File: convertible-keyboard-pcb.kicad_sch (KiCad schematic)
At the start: 216 parts, among them SW1 SW_MX_LED, SW10 SW_MX_LED, SW100 SW_MX_LED, SW101 SW_MX_LED, SW102 SW_MX_LED, SW103 SW_MX_LED, SW104 SW_MX_LED, SW105 SW_MX_LED, SW106 SW_Push, SW107 SW_MX_LED, SW108 SW_MX_LED, SW11 SW_MX_LED, SW12 SW_MX_LED, SW13 SW_MX_LED, SW14 SW_MX_LED, SW15 SW_MX_LED, SW16 SW_MX_LED, SW17 SW_MX_LED, SW18 SW_MX_LED, SW19 SW_MX_LED, SW2 SW_MX_LED, SW20 SW_MX_LED, SW21 SW_MX_LED, SW22 SW_MX_LED, SW23 SW_MX_LED, SW24 SW_MX_LED, SW25 SW_MX_LED, SW26 SW_MX_LED, SW27 SW_MX_LED, SW28 SW_MX_LED, SW29 SW_MX_LED, SW3 SW_MX_LED, SW30 SW_MX_LED, SW31 SW_MX_LED, SW32 SW_MX_LED, SW33 SW_MX_LED, SW34 SW_MX_LED, SW35 SW_MX_LED, SW36 SW_MX_LED, SW37 SW_MX_LED, SW38 SW_MX_LED, SW39 SW_MX_LED, SW4 SW_MX_LED, SW40 SW_MX_LED, SW41 SW_MX_LED, SW42 SW_MX_LED, SW43 SW_MX_LED, SW44 SW_MX_LED, SW45 SW_MX_LED, SW46 SW_MX_LED, SW47 SW_MX_LED, SW48 SW_MX_LED, SW49 SW_MX_LED, SW5 SW_MX_LED, SW50 SW_MX_LED, SW51 SW_MX_LED, SW52 SW_MX_LED, SW53 SW_MX_LED, SW54 SW_MX_LED, SW55 SW_MX_LED, SW56 SW_MX_LED, SW57 SW_MX_LED, SW58 SW_MX_LED, SW59 SW_MX_LED, SW6 SW_MX_LED, SW60 SW_MX_LED, SW61 SW_MX_LED, SW62 SW_MX_LED, SW63 SW_MX_LED, SW64 SW_MX_LED, SW65 SW_MX_LED, SW66 SW_MX_LED, SW67 SW_MX_LED, SW68 SW_MX_LED, SW69 SW_MX_LED, SW7 SW_MX_LED, SW70 SW_MX_LED, SW71 SW_MX_LED, SW72 SW_MX_LED, SW73 SW_MX_LED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

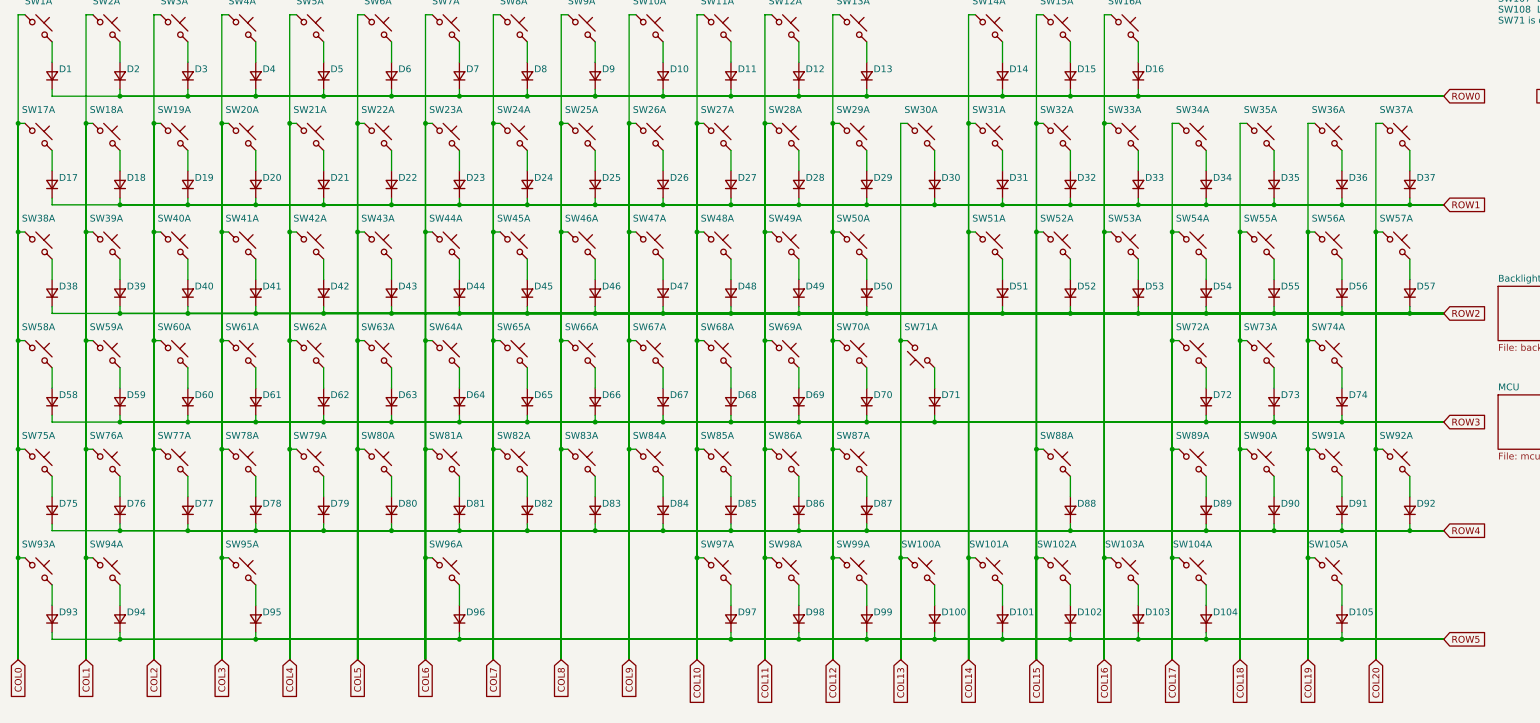
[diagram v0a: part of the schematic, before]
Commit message: Blattgröße, Titelblöcke und Kommentare angepasst
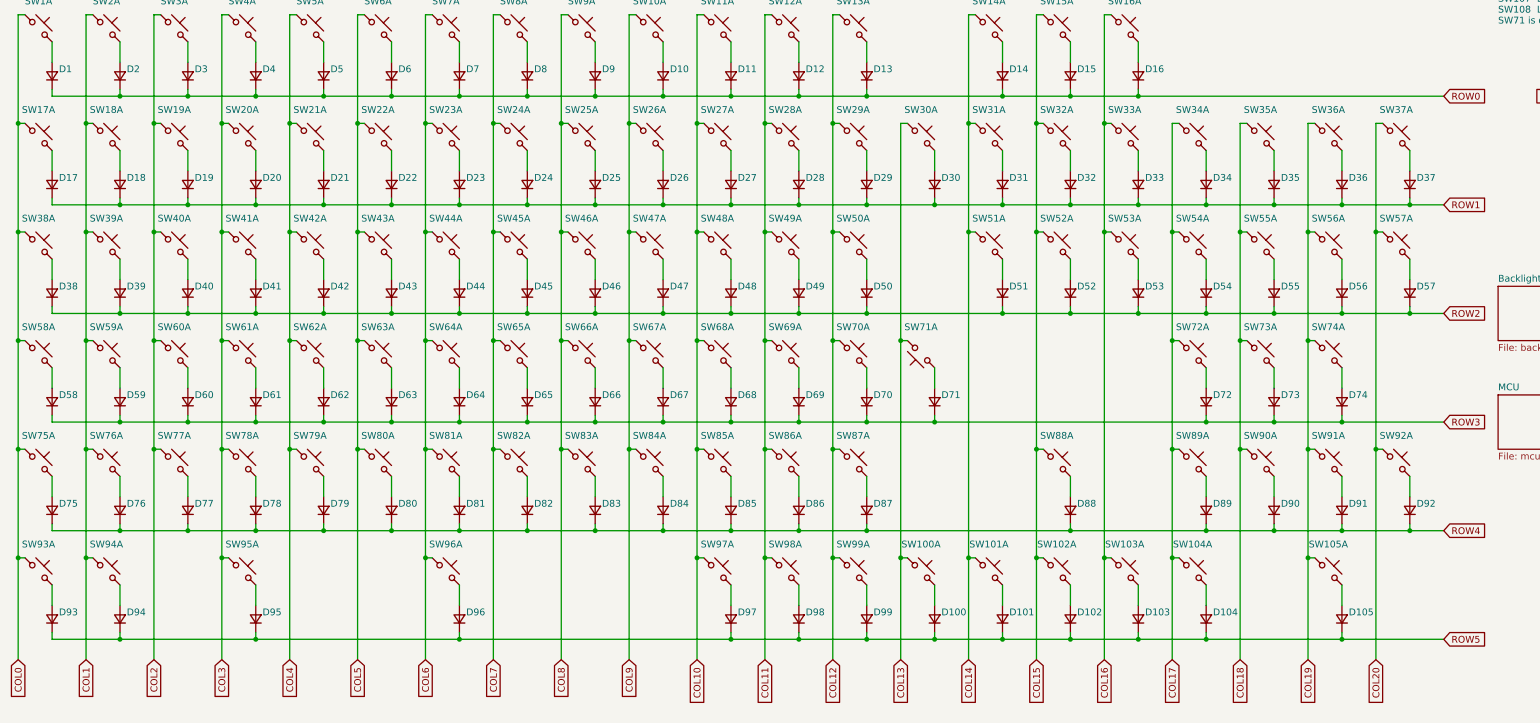
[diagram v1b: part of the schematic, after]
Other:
- company: (none) -> Philipp Weber
- title: convertible-keyboard-pcb -> Key-Matrix
